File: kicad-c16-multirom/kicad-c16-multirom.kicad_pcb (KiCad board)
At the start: 2 copper layers, 55.9 x 42 mm, 13 parts, among them J1 Conn_01x02_Pin, J2 Conn_01x02_Pin, J3 Conn_01x01_Pin, J4 Conn_01x01_Pin, J5 Conn_01x01_Pin, U1 ATtiny85-20P, U2 74LS00, U3 27C512, U4 27C512

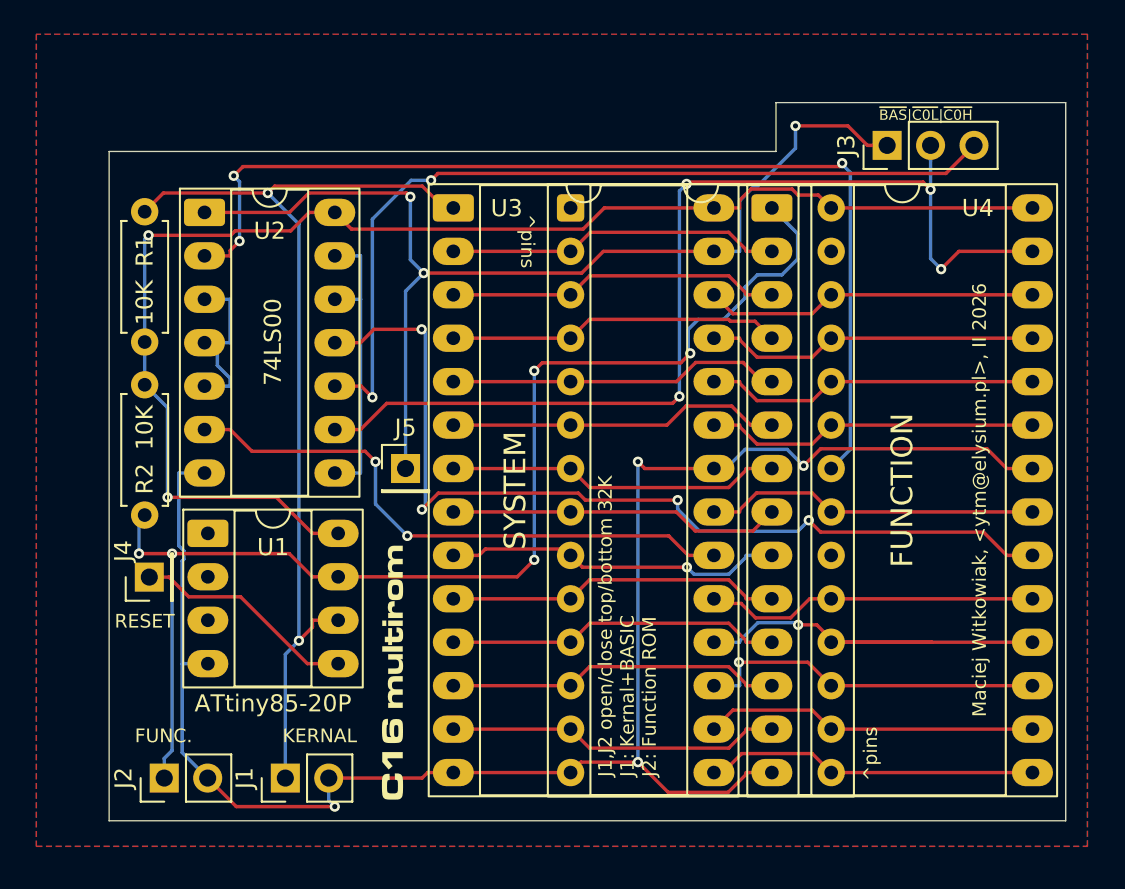
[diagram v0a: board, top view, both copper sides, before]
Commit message: correct reference image placement, lock footprints for precision pins that go down to the mainboard
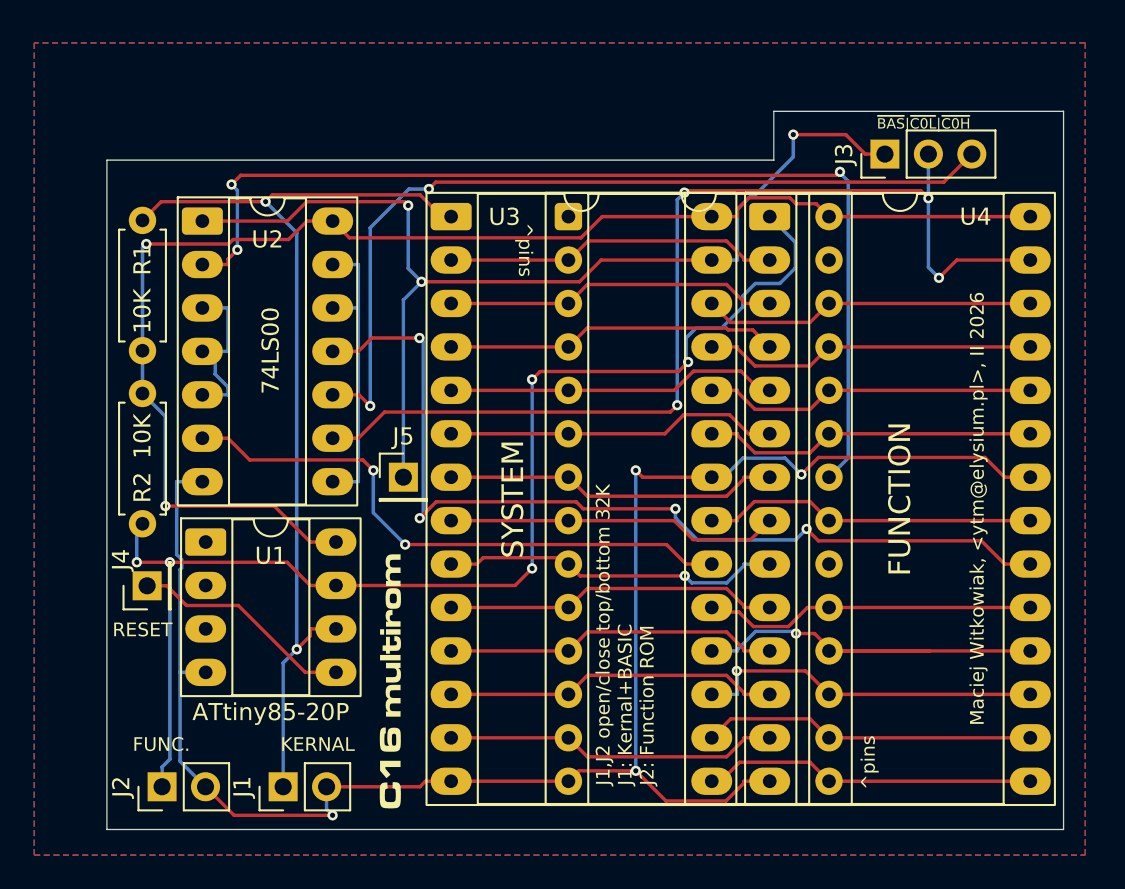
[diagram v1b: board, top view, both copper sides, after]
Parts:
- moved J5 0.52 mm to (148.2, 73.4)
- moved J3 0.52 mm to (176.4, 54.5)
- moved J1 0.52 mm to (141.2, 91.5)
- moved R1 0.52 mm to (133.0, 66.0)
- moved R2 0.52 mm to (133.0, 68.5)
- moved SOCKET_U4 0.52 mm to (157.9, 58.2)
- moved U1 0.52 mm to (136.6, 77.2)
- moved U2 0.52 mm to (136.5, 58.4)
- moved U3 0.52 mm to (151.0, 58.2)
- moved kibuzzard-6987CFF9 0.52 mm to (147.4, 85.3)
- moved J2 0.52 mm to (134.1, 91.5)
- moved J4 0.52 mm to (133.2, 79.8)
- moved U4 0.52 mm to (169.6, 58.2)
